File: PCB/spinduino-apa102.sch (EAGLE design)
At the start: 27 parts

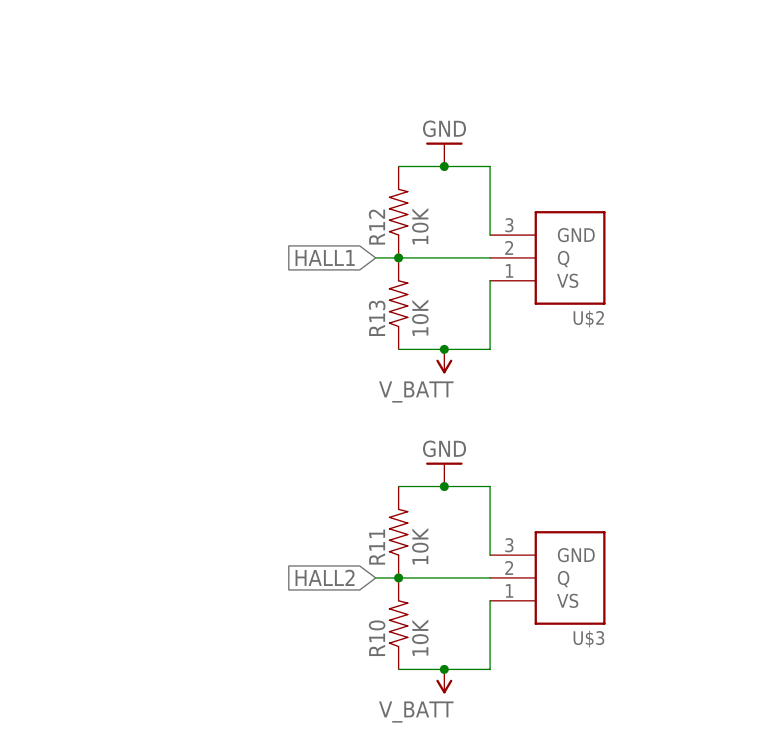
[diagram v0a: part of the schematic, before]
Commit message: fix: remove redundant resistor
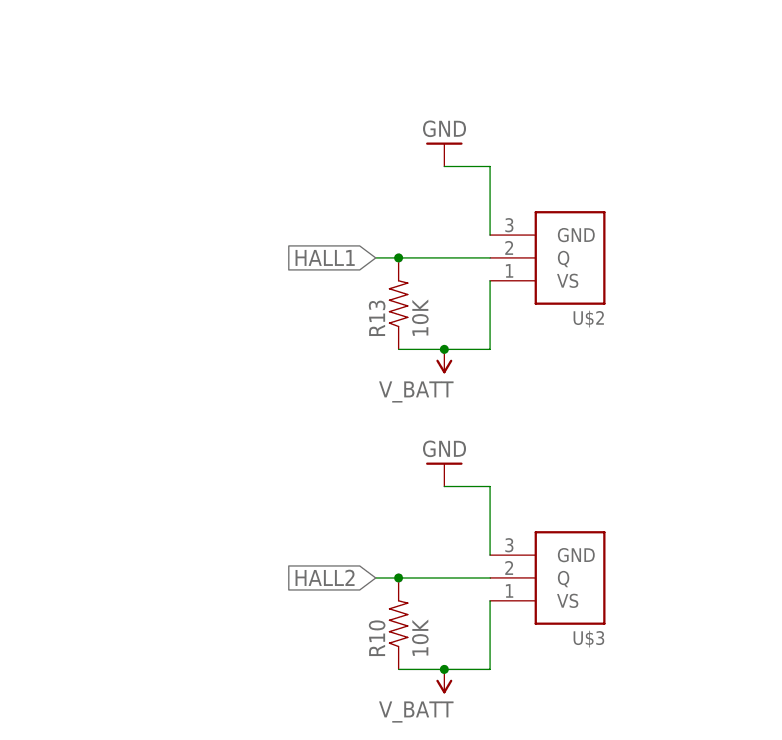
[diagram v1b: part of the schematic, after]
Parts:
- removed R11, R12: 10K, SparkFun-Resistors:10KOHM-1/10W-1%(0603)0603
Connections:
- net GND: no longer R11.2, R12.2
- net HALL1: no longer R12.1
- net HALL2: no longer R11.1
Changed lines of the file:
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@@
 <part name="GND9" library="ng-beacon" deviceset="GND" device=""/>
 <part name="R10" library="SparkFun-Resistors" deviceset="10KOHM-1/10W-1%(0603)" device="0603" value="10K"/>
-<part name="R11" library="SparkFun-Resistors" deviceset="10KOHM-1/10W-1%(0603)" device="0603" value="10K"/>
 <part name="SUPPLY2" library="SparkFun-Aesthetics" deviceset="V_BATT" device=""/>
 <part name="SUPPLY3" library="SparkFun-Aesthetics" deviceset="V_BATT" device=""/>
@@
 <part name="SUPPLY4" library="SparkFun-Aesthetics" deviceset="V_BATT" device=""/>
 <part name="GND10" library="ng-beacon" deviceset="GND" device=""/>
-<part name="R12" library="SparkFun-Resistors" deviceset="10KOHM-1/10W-1%(0603)" device="0603" value="10K"/>
 <part name="R13" library="SparkFun-Resistors" deviceset="10KOHM-1/10W-1%(0603)" device="0603" value="10K"/>
 <part name="C1" library="SparkFun-Capacitors" deviceset="1.0UF-16V-10%(0603)" device="" value="1.0uF"/>
@@
 <instance part="GND9" gate="1" x="167.64" y="12.7" rot="R180"/>
 <instance part="R10" gate="G$1" x="162.56" y="-5.08" rot="R90"/>
-<instance part="R11" gate="G$1" x="162.56" y="5.08" rot="R90"/>
 <instance part="SUPPLY2" gate="G$1" x="-10.16" y="55.88" rot="R90"/>
 <instance part="SUPPLY3" gate="G$1" x="-10.16" y="73.66" rot="R90"/>
@@
 <instance part="SUPPLY4" gate="G$1" x="68.58" y="22.86" rot="R180"/>
 <instance part="GND10" gate="1" x="167.64" y="48.26" rot="R180"/>
-<instance part="R12" gate="G$1" x="162.56" y="40.64" rot="R90"/>
 <instance part="R13" gate="G$1" x="162.56" y="30.48" rot="R90"/>
 <instance part="C1" gate="G$1" x="33.02" y="111.76" rot="R90"/>
@@
 </segment>
 <segment>
-<pinref part="R11" gate="G$1" pin="2"/>
-<wire x1="162.56" y1="10.16" x2="167.64" y2="10.16" width="0.1524" layer="91"/>
 <pinref part="U$3" gate="G$1" pin="GND"/>
 <wire x1="167.64" y1="10.16" x2="172.72" y2="10.16" width="0.1524" layer="91"/>
 <wire x1="172.72" y1="10.16" x2="172.72" y2="2.54" width="0.1524" layer="91"/>
 <pinref part="GND9" gate="1" pin="GND"/>
-<junction x="167.64" y="10.16"/>
-</segment>
-<segment>
-<pinref part="R12" gate="G$1" pin="2"/>
-<wire x1="162.56" y1="45.72" x2="167.64" y2="45.72" width="0.1524" layer="91"/>
+</segment>
+<segment>
 <wire x1="167.64" y1="45.72" x2="172.72" y2="45.72" width="0.1524" layer="91"/>
 <pinref part="GND10" gate="1" pin="GND"/>
-<junction x="167.64" y="45.72"/>
 <wire x1="172.72" y1="45.72" x2="172.72" y2="38.1" width="0.1524" layer="91"/>
 <pinref part="U$2" gate="G$1" pin="GND"/>
@@
 <wire x1="172.72" y1="35.56" x2="162.56" y2="35.56" width="0.1524" layer="91"/>
 <label x="160.02" y="35.56" size="1.778" layer="95" rot="R180" xref="yes"/>
-<pinref part="R12" gate="G$1" pin="1"/>
 <wire x1="162.56" y1="35.56" x2="160.02" y2="35.56" width="0.1524" layer="91"/>
 <junction x="162.56" y="35.56"/>
@@
 <wire x1="162.56" y1="0" x2="160.02" y2="0" width="0.1524" layer="91"/>
 <junction x="162.56" y="0"/>
-<pinref part="R11" gate="G$1" pin="1"/>
 </segment>
 </net>

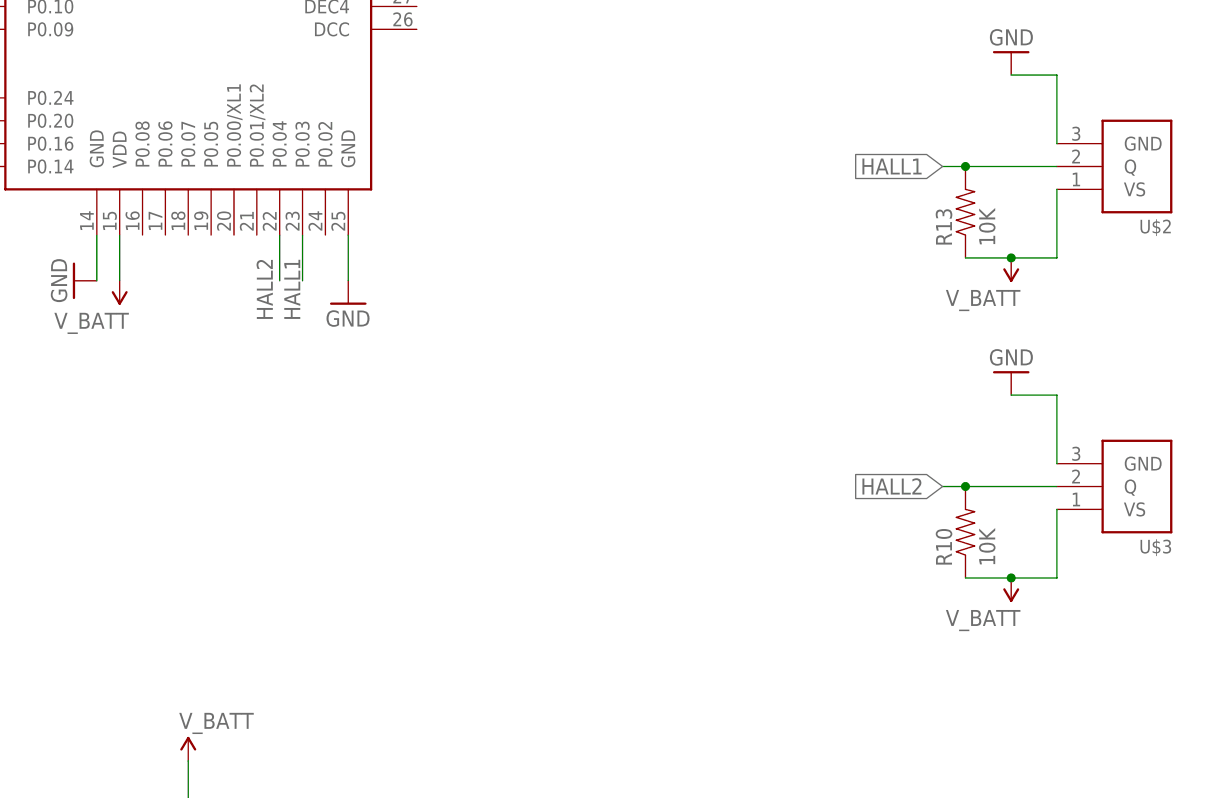
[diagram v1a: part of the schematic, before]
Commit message: Make hall effect sensors powered by CPU
This will help with standby power consumption
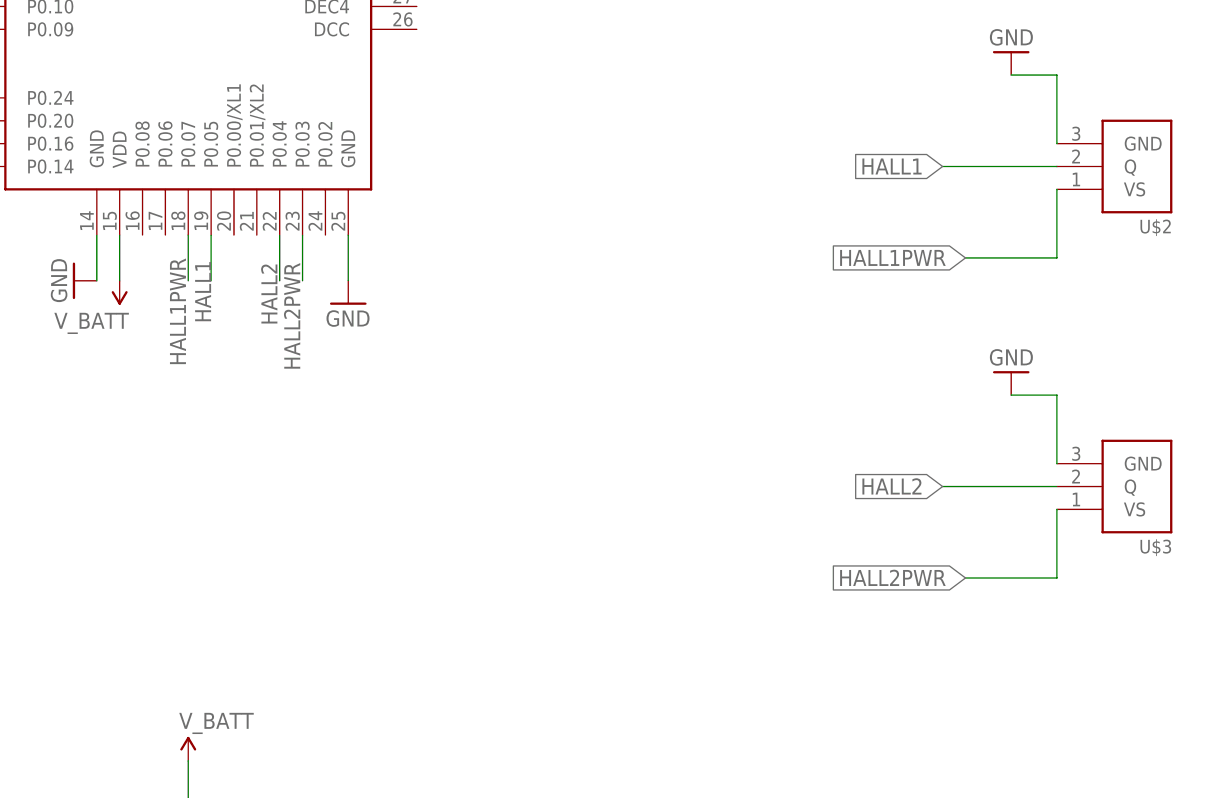
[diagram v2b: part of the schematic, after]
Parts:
- removed R10, R13: 10K, SparkFun-Resistors:10KOHM-1/10W-1%(0603)0603
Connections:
- new net HALL1PWR: U$1.P0.07, U$2.VS
- new net HALL2PWR: U$1.P0.03, U$3.VS
- net HALL1: now also U$1.P0.05; no longer R13.2, U$1.P0.03
- net HALL2: no longer R10.2
- net V_BATT: no longer R10.1, R13.1, U$2.VS, U$3.VS
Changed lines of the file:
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@@
 <part name="U$3" library="uri" deviceset="TLE4946-2K" device="SMD"/>
 <part name="GND9" library="ng-beacon" deviceset="GND" device=""/>
-<part name="R10" library="SparkFun-Resistors" deviceset="10KOHM-1/10W-1%(0603)" device="0603" value="10K"/>
 <part name="SUPPLY2" library="SparkFun-Aesthetics" deviceset="V_BATT" device=""/>
 <part name="SUPPLY3" library="SparkFun-Aesthetics" deviceset="V_BATT" device=""/>
@@
 <part name="SUPPLY4" library="SparkFun-Aesthetics" deviceset="V_BATT" device=""/>
 <part name="GND10" library="ng-beacon" deviceset="GND" device=""/>
-<part name="R13" library="SparkFun-Resistors" deviceset="10KOHM-1/10W-1%(0603)" device="0603" value="10K"/>
 <part name="C1" library="SparkFun-Capacitors" deviceset="1.0UF-16V-10%(0603)" device="" value="1.0uF"/>
 <part name="C2" library="SparkFun-Capacitors" deviceset="0.1UF-25V-5%(0603)" device="" value="0.1uF"/>
@@
 <part name="S1" library="SparkFun-Electromechanical" deviceset="SWITCH-MOMENTARY-2" device="SMD-1101NE"/>
 <part name="GND13" library="ng-beacon" deviceset="GND" device=""/>
-<part name="SUPPLY1" library="SparkFun-Aesthetics" deviceset="V_BATT" device=""/>
-<part name="SUPPLY6" library="SparkFun-Aesthetics" deviceset="V_BATT" device=""/>
 </parts>
 <sheets>
@@
 <instance part="U$3" gate="G$1" x="180.34" y="0" rot="R180"/>
 <instance part="GND9" gate="1" x="167.64" y="12.7" rot="R180"/>
-<instance part="R10" gate="G$1" x="162.56" y="-5.08" rot="R90"/>
 <instance part="SUPPLY2" gate="G$1" x="-10.16" y="55.88" rot="R90"/>
 <instance part="SUPPLY3" gate="G$1" x="-10.16" y="73.66" rot="R90"/>
@@
 <instance part="SUPPLY4" gate="G$1" x="68.58" y="22.86" rot="R180"/>
 <instance part="GND10" gate="1" x="167.64" y="48.26" rot="R180"/>
-<instance part="R13" gate="G$1" x="162.56" y="30.48" rot="R90"/>
 <instance part="C1" gate="G$1" x="33.02" y="111.76" rot="R90"/>
 <instance part="C2" gate="G$1" x="33.02" y="119.38" rot="R90"/>
@@
 <instance part="S1" gate="G$1" x="43.18" y="63.5" rot="R180"/>
 <instance part="GND13" gate="1" x="33.02" y="63.5" rot="R270"/>
-<instance part="SUPPLY1" gate="G$1" x="167.64" y="-10.16" rot="R180"/>
-<instance part="SUPPLY6" gate="G$1" x="167.64" y="25.4" rot="R180"/>
 </instances>
 <busses>
@@
 <net name="HALL1" class="0">
 <segment>
-<pinref part="U$1" gate="G$1" pin="P0.03"/>
-<wire x1="88.9" y1="27.94" x2="88.9" y2="22.86" width="0.1524" layer="91"/>
-<label x="86.868" y="25.4" size="1.778" layer="95" rot="R270"/>
-</segment>
-<segment>
 <pinref part="U$2" gate="G$1" pin="Q"/>
-<wire x1="172.72" y1="35.56" x2="162.56" y2="35.56" width="0.1524" layer="91"/>
+<wire x1="172.72" y1="35.56" x2="160.02" y2="35.56" width="0.1524" layer="91"/>
 <label x="160.02" y="35.56" size="1.778" layer="95" rot="R180" xref="yes"/>
-<wire x1="162.56" y1="35.56" x2="160.02" y2="35.56" width="0.1524" layer="91"/>
-<junction x="162.56" y="35.56"/>
-<pinref part="R13" gate="G$1" pin="2"/>
+</segment>
+<segment>
+<pinref part="U$1" gate="G$1" pin="P0.05"/>
+<wire x1="78.74" y1="27.94" x2="78.74" y2="22.86" width="0.1524" layer="91"/>
+<label x="76.962" y="25.146" size="1.778" layer="95" rot="R270"/>
 </segment>
 </net>
 <net name="HALL2" class="0">
+<segment>
+<pinref part="U$3" gate="G$1" pin="Q"/>
+<wire x1="172.72" y1="0" x2="160.02" y2="0" width="0.1524" layer="91"/>
+<label x="160.02" y="0" size="1.778" layer="95" rot="R180" xref="yes"/>
+</segment>
 <segment>
 <pinref part="U$1" gate="G$1" pin="P0.04"/>
 <wire x1="86.36" y1="27.94" x2="86.36" y2="22.86" width="0.1524" layer="91"/>
-<label x="83.82" y="25.4" size="1.778" layer="95" rot="R270"/>
-</segment>
-<segment>
-<pinref part="U$3" gate="G$1" pin="Q"/>
-<wire x1="172.72" y1="0" x2="162.56" y2="0" width="0.1524" layer="91"/>
-<label x="160.02" y="0" size="1.778" layer="95" rot="R180" xref="yes"/>
-<pinref part="R10" gate="G$1" pin="2"/>
-<wire x1="162.56" y1="0" x2="160.02" y2="0" width="0.1524" layer="91"/>
-<junction x="162.56" y="0"/>
+<label x="84.328" y="24.892" size="1.778" layer="95" rot="R270"/>
 </segment>
 </net>
@@
 <wire x1="137.16" y1="73.66" x2="134.62" y2="73.66" width="0.1524" layer="91"/>
 </segment>
-<segment>
-<pinref part="U$3" gate="G$1" pin="VS"/>
-<wire x1="172.72" y1="-2.54" x2="172.72" y2="-10.16" width="0.1524" layer="91"/>
-<pinref part="R10" gate="G$1" pin="1"/>
-<wire x1="172.72" y1="-10.16" x2="167.64" y2="-10.16" width="0.1524" layer="91"/>
-<pinref part="SUPPLY1" gate="G$1" pin="V_BATT"/>
-<wire x1="167.64" y1="-10.16" x2="162.56" y2="-10.16" width="0.1524" layer="91"/>
-<junction x="167.64" y="-10.16"/>
-</segment>
-<segment>
-<wire x1="172.72" y1="33.02" x2="172.72" y2="25.4" width="0.1524" layer="91"/>
-<pinref part="R13" gate="G$1" pin="1"/>
-<wire x1="172.72" y1="25.4" x2="167.64" y2="25.4" width="0.1524" layer="91"/>
-<pinref part="U$2" gate="G$1" pin="VS"/>
-<pinref part="SUPPLY6" gate="G$1" pin="V_BATT"/>
-<wire x1="167.64" y1="25.4" x2="162.56" y2="25.4" width="0.1524" layer="91"/>
-<junction x="167.64" y="25.4"/>
-</segment>
 </net>
 <net name="SWCLK" class="0">
@@
 </segment>
 </net>
+<net name="HALL1PWR" class="0">
+<segment>
+<wire x1="172.72" y1="33.02" x2="172.72" y2="25.4" width="0.1524" layer="91"/>
+<pinref part="U$2" gate="G$1" pin="VS"/>
+<wire x1="172.72" y1="25.4" x2="162.56" y2="25.4" width="0.1524" layer="91"/>
+<label x="162.56" y="25.4" size="1.778" layer="95" rot="R180" xref="yes"/>
+</segment>
+<segment>
+<pinref part="U$1" gate="G$1" pin="P0.07"/>
+<wire x1="76.2" y1="27.94" x2="76.2" y2="22.86" width="0.1524" layer="91"/>
+<label x="74.168" y="25.4" size="1.778" layer="95" rot="R270"/>
+</segment>
+</net>
+<net name="HALL2PWR" class="0">
+<segment>
+<pinref part="U$3" gate="G$1" pin="VS"/>
+<wire x1="172.72" y1="-2.54" x2="172.72" y2="-10.16" width="0.1524" layer="91"/>
+<wire x1="172.72" y1="-10.16" x2="162.56" y2="-10.16" width="0.1524" layer="91"/>
+<label x="162.56" y="-10.16" size="1.778" layer="95" rot="R180" xref="yes"/>
+</segment>
+<segment>
+<pinref part="U$1" gate="G$1" pin="P0.03"/>
+<wire x1="88.9" y1="27.94" x2="88.9" y2="22.86" width="0.1524" layer="91"/>
+<label x="86.868" y="24.892" size="1.778" layer="95" rot="R270"/>
+</segment>
+</net>
